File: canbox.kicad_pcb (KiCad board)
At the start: 2 copper layers, 80 x 50 mm, 108 parts, among them J1 Conn_ARM_SWD_NXP, J2 Screw_Terminal_01x02, J3 Screw_Terminal_01x02, J4 Conn_ARM_JTAG_SWD_20, J5 DB9_Male, J7 USB_B_Micro, K2 FTR-K3AB005W, U1 LPC54616J512, U11 MP1582, U3 TJA1102SHN, U5 TJA1051T, U6 TLV70233_SOT23-5, U7 KeyMatrix, U8 ULN2003ADRG3, Y1 12MHz, Y2 32.768k, Y3 25Mhz

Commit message: Fix few bugs, review design
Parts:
- added R11: NC, Resistor_SMD:R_0805_2012Metric_Pad1.15x1.40mm_HandSolder, F.Cu at (49.5, 117.3)
- D1: footprint Package_TO_SOT_SMD:SOT-143 -> Package_TO_SOT_SMD:SOT-143_Handsoldering
- moved L5 1.22 mm to (49.2, 112.5)
- moved C24 0.76 mm to (102.4, 130.0), turned to 180 degrees
- moved L3 0.73 mm to (105.9, 125.6), turned to 90 degrees
- moved R12 0.45 mm to (52.3, 110.9), turned to 90 degrees
- turned D5 to 180 degrees
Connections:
- D5 pad 1: GND -> Net-(C45-Pad1)
- D5 pad 2: Net-(C45-Pad1) -> GND
- J5 pad 1: /CAN/CAN_L -> (no net)
- J5 pad 2: (no net) -> /CAN/CAN_L
- J5 pad 7: (no net) -> /CAN/CAN_H
- J5 pad 8: /CAN/CAN_H -> (no net)
- L5 pad 3: /CAN/CAN_L -> Net-(L5-Pad3)
- L5 pad 4: Net-(L5-Pad4) -> /CAN/CAN_L
- R13 pad 1: Net-(L5-Pad4) -> Net-(L5-Pad3)
- U3 pad 17: /Ethernet/TRX_0_T_N -> /Ethernet/TRX_0_T_P
- U3 pad 18: /Ethernet/TRX_0_T_P -> /Ethernet/TRX_0_T_N
- U3 pad 48: (no net) -> +3V3
- U5 pad 5: (no net) -> Net-(R11-Pad2)
- U5 pad 6: Net-(L5-Pad4) -> Net-(L5-Pad3)
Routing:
- net GND: track 949.1 -> 879.2 mm, vias 59 -> 53
- net 5V: track 192.2 -> 221.6 mm
- net Net-(L5-Pad3): track 0.00 -> 16.7 mm, vias 0 -> 1
- net Net-(L5-Pad4): track 15.6 -> 0.00 mm, vias 1 -> 0
- net /Ethernet/TRX_0_T_N: track 5.14 -> 11.4 mm
- net /CAN/CAN_H: track 24.4 -> 29.6 mm
- net /MCU/3V3_LC: track 77.8 -> 82.6 mm, vias 4 -> 5
- net /Ethernet/TRX_0_P: track 2.98 -> 7.43 mm
- net Net-(R11-Pad2): track 0.00 -> 4.22 mm
- net /Ethernet/TRX_0_T_P: track 6.50 -> 9.89 mm
- net /PowerSupply/D+: track 41.3 -> 38.1 mm
- net /CAN/CAN_L: track 40.3 -> 37.2 mm
- net Net-(C22-Pad1): track 30.2 -> 33.2 mm
- net /Ethernet/TRX_0_N: track 14.1 -> 11.2 mm
- net Net-(L5-Pad2): track 14.1 -> 11.2 mm
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
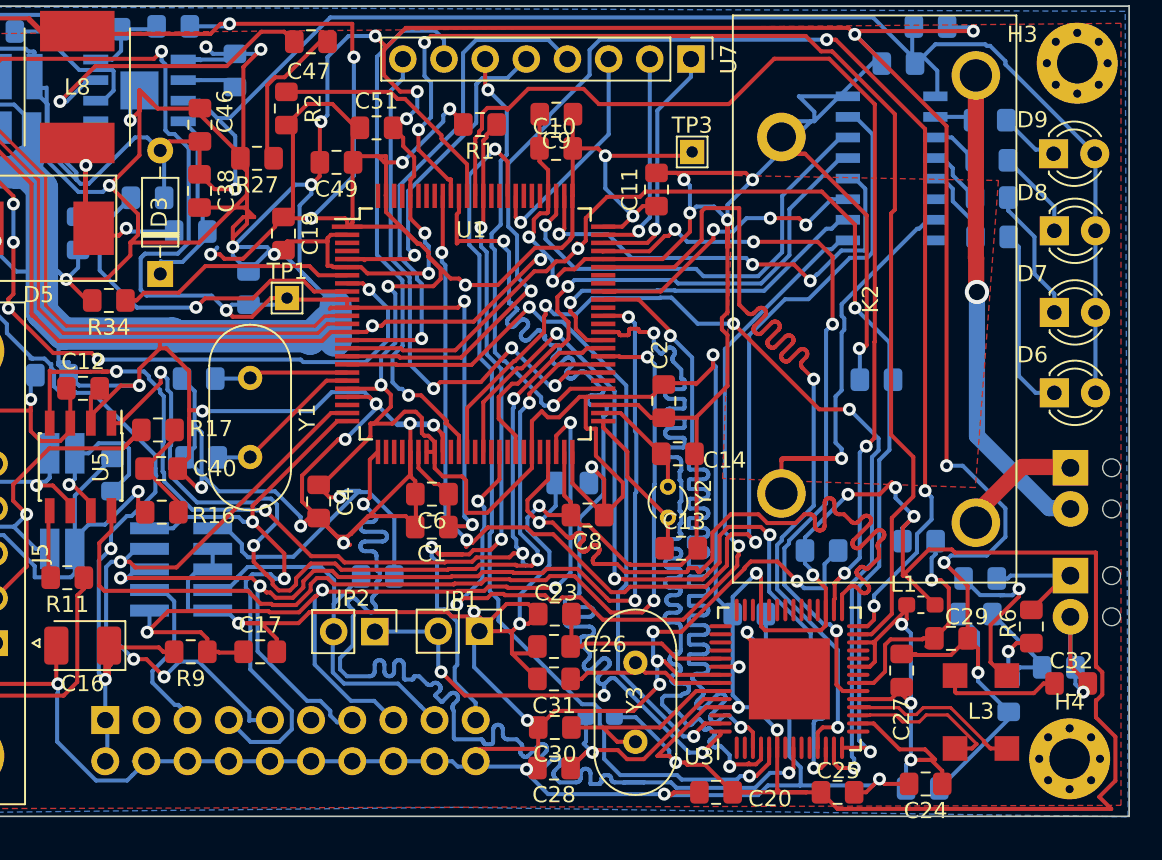
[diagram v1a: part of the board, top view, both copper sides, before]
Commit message: Add solder jumper for termination.
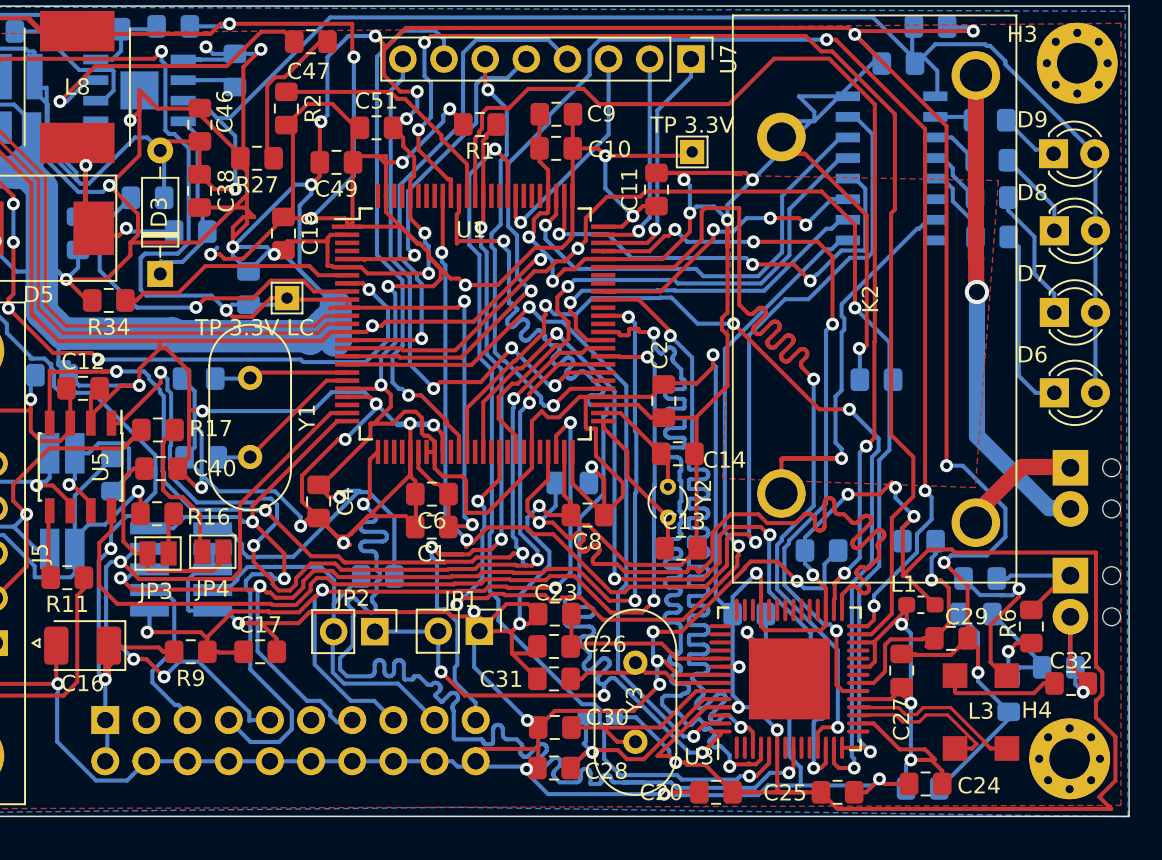
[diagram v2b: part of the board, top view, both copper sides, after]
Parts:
- added JP3: Jumper_NC_Small-Device, Jumper:SolderJumper-2_P1.3mm_Open_Pad1.0x1.5mm, F.Cu at (55.1, 115.8)
- added JP4: Jumper_NC_Small-Device, Jumper:SolderJumper-2_P1.3mm_Open_Pad1.0x1.5mm, F.Cu at (58.5, 115.7)
- TP 3.3V: renamed from TP3
- TP 3.3V LC: renamed from TP1
- moved R16 0.31 mm to (55.0, 113.3)
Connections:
- R16 pad 2: Net-(C40-Pad1) -> Net-(JP3-Pad2)
- R17 pad 2: Net-(C40-Pad1) -> Net-(JP4-Pad1)
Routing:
- net Net-(JP4-Pad1): track 0.00 -> 9.73 mm
- net Net-(C40-Pad1): track 6.72 -> 13.7 mm
- net Net-(C17-Pad1): track 59.3 -> 55.9 mm
- net Net-(J1-Pad4): track 39.5 -> 42.6 mm
- net Net-(JP3-Pad2): track 0.00 -> 2.58 mm

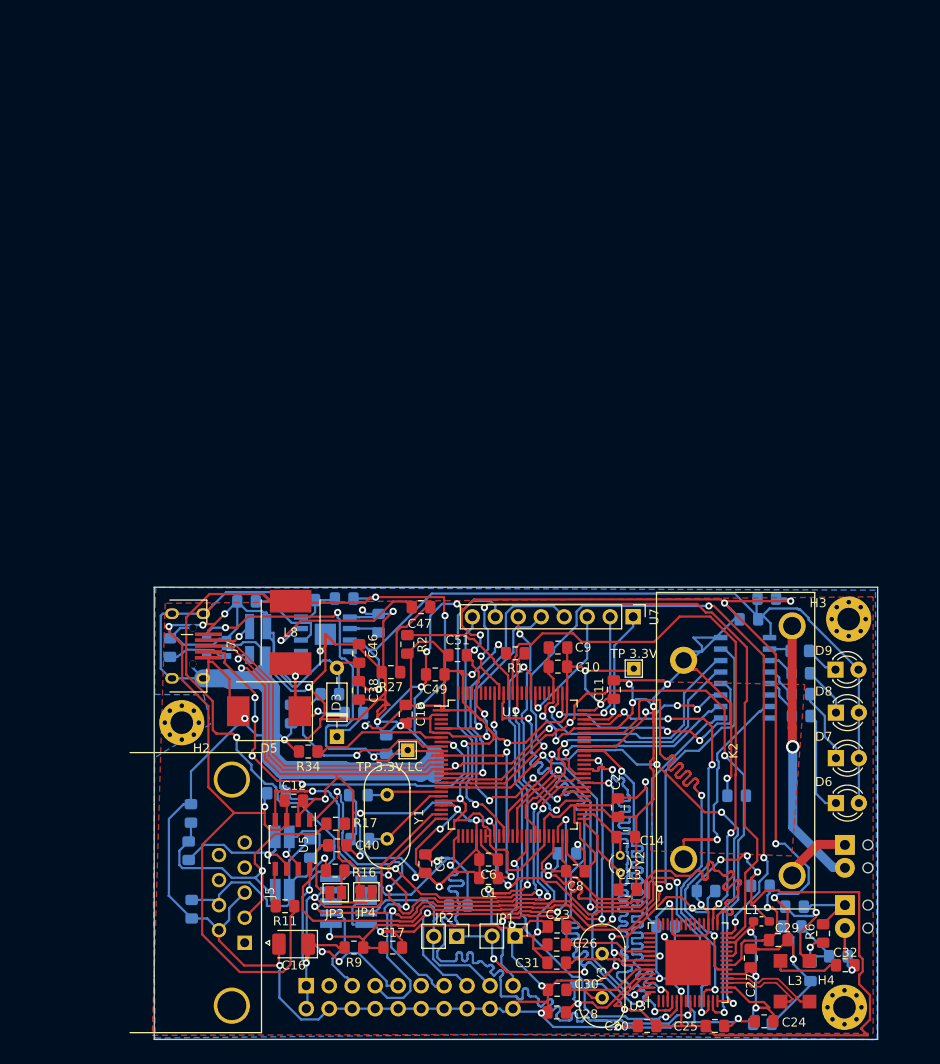
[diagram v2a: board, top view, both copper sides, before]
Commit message: V3 bigger board, RMII instrumentation, inverter
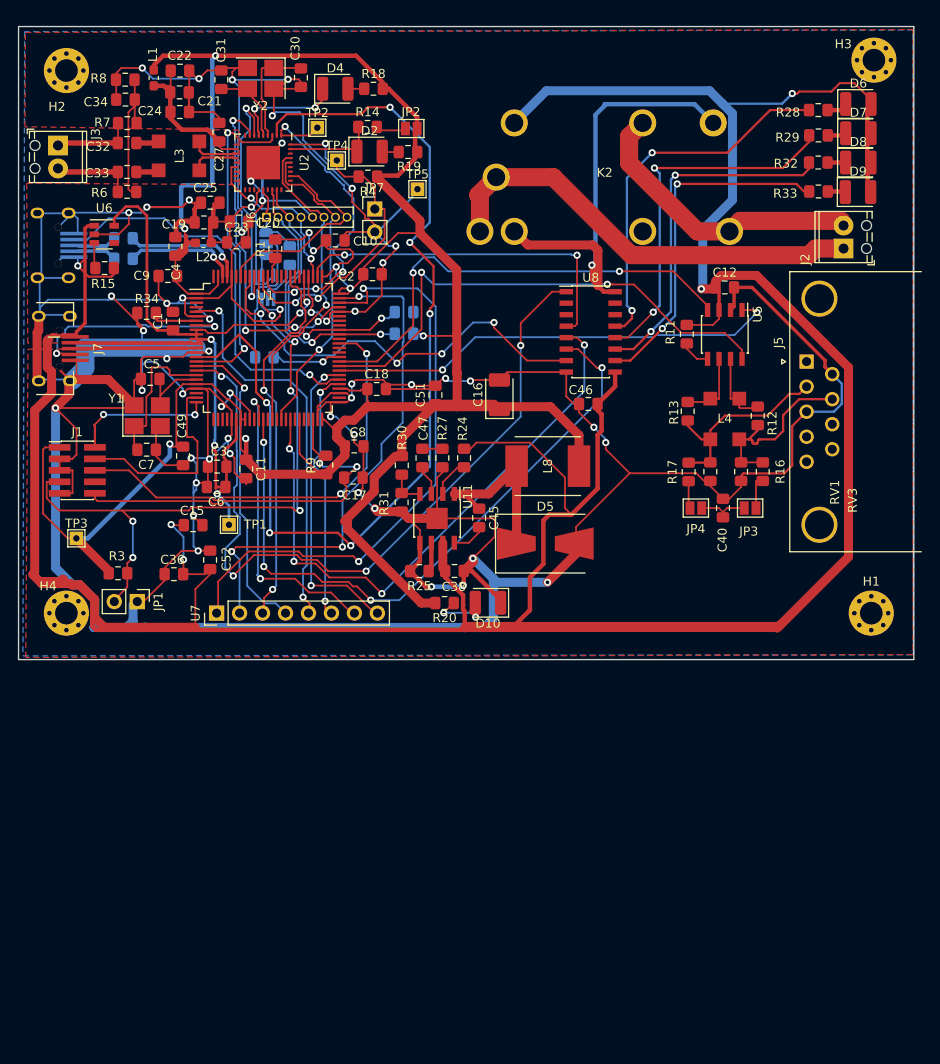
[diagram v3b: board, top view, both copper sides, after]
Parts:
- removed C13, C14: 22p, Capacitor_SMD:C_0805_2012Metric_Pad1.15x1.40mm_HandSolder
- removed C26: 10n, Capacitor_SMD:C_0805_2012Metric_Pad1.15x1.40mm_HandSolder
- removed C28, C29: 100n, Capacitor_SMD:C_0805_2012Metric_Pad1.15x1.40mm_HandSolder
- removed D1: PRTR5V0U2X, Package_TO_SOT_SMD:SOT-143_Handsoldering
- removed D3: 1N4148, Diode_THT:D_DO-35_SOD27_P7.62mm_Horizontal
- removed L5: DLW43MH201XK2L, cypress:DLW43MH201XK2L
- removed R26: 124k, Resistor_SMD:R_0805_2012Metric_Pad1.15x1.40mm_HandSolder
- removed TP 3.3V: TestPoint, TestPoint:TestPoint_THTPad_1.5x1.5mm_Drill0.7mm
- removed TP 3.3V LC: TestPoint, TestPoint:TestPoint_THTPad_1.5x1.5mm_Drill0.7mm
- removed Y3: 25Mhz, Crystal:Crystal_HC49-4H_Vertical
- added D10: LED, LED_SMD:LED_1210_3225Metric, F.Cu at (71.9, 83.7)
- added D2: LED, LED_SMD:LED_1210_3225Metric, F.Cu at (58.8, 33.8)
- added D4: LED, LED_SMD:LED_1210_3225Metric, F.Cu at (55.0, 26.9)
- added H1: H, MountingHole:MountingHole_2.5mm_Pad_Via, F.Cu at (114.3, 84.9)
- added J6: Conn_01x08_Female, Connector_PinHeader_1.27mm:PinHeader_1x08_P1.27mm_Vertical_RMII, F.Cu at (47.4, 41.1)
- added JP5: Jumper_3_Bridged12, Jumper:SolderJumper-3_P1.3mm_Open_RoundedPad1.0x1.5mm, B.Cu at (47.4, 44.0)
- added JP7: MDIO, Connector_PinHeader_2.54mm:PinHeader_1x02_P2.54mm_Vertical, F.Cu at (59.4, 40.2)
- added L4: AE2002, Inductor_SMD:L_CMC_1812, F.Cu at (98.1, 63.4)
- added R14: 2.49k, Resistor_SMD:R_0805_2012Metric_Pad1.15x1.40mm_HandSolder, F.Cu at (58.6, 31.1)
- added R18: 100, Resistor_SMD:R_0805_2012Metric_Pad1.15x1.40mm_HandSolder, F.Cu at (59.3, 26.9)
- added R19: 100, Resistor_SMD:R_0805_2012Metric_Pad1.15x1.40mm_HandSolder, F.Cu at (63.1, 33.9)
- added R20: 100, Resistor_SMD:R_0805_2012Metric_Pad1.15x1.40mm_HandSolder, F.Cu at (67.1, 83.7)
- added R21: 33, Resistor_SMD:R_0805_2012Metric_Pad1.15x1.40mm_HandSolder, B.Cu at (31.6, 43.4)
- added R22: 33, Resistor_SMD:R_0805_2012Metric_Pad1.15x1.40mm_HandSolder, B.Cu at (47.2, 56.6)
- added TP1: TestPoint, TestPoint:TestPoint_THTPad_1.5x1.5mm_Drill0.7mm, F.Cu at (43.3, 75.1)
- added TP2: MDC, TestPoint:TestPoint_THTPad_1.5x1.5mm_Drill0.7mm, F.Cu at (53.0, 31.2)
- added TP3: TestPoint, TestPoint:TestPoint_THTPad_1.5x1.5mm_Drill0.7mm, F.Cu at (26.4, 76.6)
- added TP4: MDIO, TestPoint:TestPoint_THTPad_1.5x1.5mm_Drill0.7mm, F.Cu at (55.2, 34.8)
- added TP5: GND, TestPoint:TestPoint_THTPad_1.5x1.5mm_Drill0.7mm, F.Cu at (64.1, 38.0)
- added U2: DP83TC811R-Q1, cypress:QFN-36_EP_6x6_Pitch0.5mm, F.Cu at (47.1, 35.0)
- C15, C18, C22, C3, C33, C34, C36, C45, C5, C52, C7, L2, R12, R13, R28, R29, R30, R32, R33, R7, RV1, RV3, U6, U8: moved to F.Cu
- C19: value 100n -> 22u
- C20, C27: value 100n -> 10n
- C21: value 100n -> 470n; moved to F.Cu
- C23: value 470n -> 470
- D5: footprint Diode_SMD:D_SMC -> Diode_SMD:D_SMB-SMC_Universal_Handsoldering
- D6, D7, D8, D9: footprint LED_THT:LED_D3.0mm -> LED_SMD:LED_1210_3225Metric
- H2, H3, H4: value MountingHole -> H
- J1: value Conn_ARM_SWD_NXP -> SWD; moved to F.Cu
- J2: value Screw_Terminal_01x02 -> RELAY; moved to F.Cu
- J3: value Screw_Terminal_01x02 -> 100BaseT1; moved to F.Cu
- J4: value Conn_ARM_JTAG_SWD_20 -> USB_B_Micro; footprint Connector_IDC:IDC-Header_2x10_P2.54mm_Vertical -> cypress:MicroUsb
- JP1: value Jumper_NC_Small -> MCD
- JP2: value Jumper_NC_Small -> SLAVE; footprint Connector_PinHeader_2.54mm:PinHeader_1x02_P2.54mm_Vertical -> Jumper:SolderJumper-2_P1.3mm_Open_Pad1.0x1.5mm
- JP3, JP4: value Jumper_NC_Small-Device -> TERM
- R1, R9: value 100k -> 124k
- R10: value 10k -> 2.49k
- R15, R24, R3, R8: value 100k -> 124k; moved to F.Cu
- R2: value 100k -> 33; moved to B.Cu
- R23: value 124k -> 33
- R25: value 200k -> 124k; moved to F.Cu
- R31: value 40.2k -> 39.2k; moved to F.Cu
- R4: value 10k -> 2.49k; moved to F.Cu
- R5: value 1k -> 2.49k
- U11: value MP1582 -> MP1582EN-LF-Z; moved to F.Cu
- U3: value TJA1102SHN -> 74LVC1G04; footprint canbox_nxp_LPC546xx:QFN-56_EP_8.5x8.5_Pitch0.5mm -> Package_TO_SOT_SMD:SOT-353_SC-70-5_Handsoldering; moved to B.Cu
- U5: value TJA1051T -> TJA1051T/3/1J
- Y1: value 12MHz -> 12MHZ; footprint Crystal:Crystal_HC49-4H_Vertical -> Crystal:Crystal_SMD_3225-4Pin_3.2x2.5mm_HandSoldering
- Y2: value 32.768k -> 25 MHz; footprint Crystal:Crystal_DS26_D2.0mm_L6.0mm_Vertical -> Crystal:Crystal_SMD_3225-4Pin_3.2x2.5mm_HandSoldering
- moved R8 124.4 mm to (31.8, 25.9), turned to 180 degrees
- moved C22 123.5 mm to (37.9, 24.9)
- moved R7 121.1 mm to (32.0, 30.7), turned to 0 degrees
- moved J3 120.9 mm to (24.4, 33.2)
- moved C32 120.7 mm to (32.0, 32.9), turned to 0 degrees
- moved C24 119.5 mm to (37.8, 29.5), turned to 0 degrees
- moved C34 117.4 mm to (31.8, 28.1)
- moved L1 115.0 mm to (35.0, 25.7), turned to 270 degrees
- moved L3 113.9 mm to (37.7, 34.3), turned to 0 degrees
- moved R6 112.5 mm to (32.0, 38.3), turned to 0 degrees
- moved C33 109.8 mm to (32.0, 36.1), turned to 180 degrees
- moved C27 108.6 mm to (42.2, 31.7)
- moved C25 106.8 mm to (41.2, 39.5), turned to 180 degrees
- moved C21 106.8 mm to (37.8, 27.3)
- moved C30 104.8 mm to (51.2, 25.7), turned to 270 degrees
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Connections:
- C1 pad 1: /MCU/3V3_LC -> /3V3_LC
- C12 pad 1: 5V -> +5V
- C15 pad 1: 5V -> +5V
- C19 pad 1: +3V3 -> /Ethernet/ETH_3V3
- C20 pad 1: +3V3 -> /Ethernet/ETH_3V3
- C21 pad 1: +3V3 -> Net-(C21-Pad1)
- C22 pad 1: Net-(C22-Pad1) -> Net-(C21-Pad1)
- C23 pad 1: Net-(C23-Pad1) -> /Ethernet/ETH_3V3
- C24 pad 1: Net-(C22-Pad1) -> Net-(C21-Pad1)
- C25 pad 1: +3V3 -> /Ethernet/ETH_3V3
- C27 pad 1: Net-(C22-Pad1) -> Net-(C21-Pad1)
- C3 pad 1: /MCU/3V3_LC -> /3V3_LC
- C36 pad 1: 5V -> +5V
- C38 pad 1: 5V -> +5V
- C46 pad 1: 5V -> +5V
- C52 pad 1: 5V -> +5V
- C6 pad 1: /MCU/3V3_LC -> /3V3_LC
- D6 pad 2: 5V -> +5V
- D7 pad 2: 5V -> +5V
- D8 pad 2: 5V -> +5V
- D9 pad 2: 5V -> +5V
- J1 pad 8: Net-(J1-Pad8) -> (no net)
- J3 pad 1: /Ethernet/TRX_CON0_N -> /Ethernet/TRX_CON0_P
- J3 pad 2: /Ethernet/TRX_CON0_P -> /Ethernet/TRX_CON0_N
- J4 pad 1: +3V3 -> +5V
- J4 pad 2: +3V3 -> /PowerSupply/Slow_D-
- J4 pad 3: (no net) -> /PowerSupply/Slow_D+
- J4 pad 4: GND -> Net-(J4-Pad4)
- J4 pad 5: Net-(J1-Pad8) -> GND
- J7 pad 1: 5V -> +5V
- JP1 pad 2: RX_DV -> Net-(J1-Pad7)
- JP2 pad 1: RX_DV -> +3V3
- JP2 pad 2: Net-(J1-Pad7) -> Net-(JP2-Pad2)
- K2 pad 1: GND -> Net-(K2-Pad1)
- K2 pad 2: Net-(K2-Pad2) -> +5V
- L1 pad 2: Net-(C22-Pad1) -> Net-(C21-Pad1)
- L2 pad 2: Net-(C28-Pad1) -> /Ethernet/ETH_3V3
- L3 pad 1: /Ethernet/TRX_0_T_P -> /Ethernet/TRX_0_P
- L3 pad 2: /Ethernet/TRX_0_T_N -> /Ethernet/TRX_0_N
- L3 pad 3: /Ethernet/TRX_0_N -> /Ethernet/TRX_0_T_N
- L3 pad 4: /Ethernet/TRX_0_P -> /Ethernet/TRX_0_T_P
- R1 pad 1: Net-(J4-Pad19) -> Net-(R1-Pad1)
- R10 pad 1: Net-(R10-Pad1) -> +3V3
- R10 pad 2: GND -> /Ethernet/RGMII_D1
- R11 pad 1: 5V -> +5V
- R15 pad 1: 5V -> +5V
- R2 pad 1: Net-(R2-Pad1) -> /PowerSupply/Slow_D-
- R2 pad 2: +3V3 -> /PowerSupply/USB0_D-
- R23 pad 1: 5V -> /Ethernet/RGMII_CLK
- R24 pad 1: 5V -> +5V
- R4 pad 2: Net-(R4-Pad2) -> /Ethernet/MDIO
- R5 pad 1: Net-(C29-Pad1) -> +3V3
- R5 pad 2: +3V3 -> /Ethernet/RGMII_DO
- U1 pad 10: /MCU/3V3_LC -> /3V3_LC
- U1 pad 11: /MCU/3V3_LC -> /3V3_LC
- U1 pad 16: Net-(R10-Pad1) -> Net-(U1-Pad16)
- U1 pad 26: Net-(U1-Pad26) -> (no net)
- U1 pad 31: /MCU/3V3_LC -> /3V3_LC
- U1 pad 39: /Ethernet/TXD0_L -> /Ethernet/RGMII_TX_D0
- U1 pad 41: Net-(U1-Pad41) -> /Ethernet/RGMII_TX_D1
- U1 pad 47: Net-(R4-Pad2) -> (no net)
- U1 pad 51: Net-(C13-Pad1) -> GND
- U1 pad 52: Net-(C14-Pad1) -> (no net)
- U1 pad 56: (no net) -> Net-(J4-Pad4)
- U1 pad 61: Net-(U1-Pad61) -> Net-(R22-Pad2)
- U1 pad 62: /Ethernet/RXD0_L -> (no net)
- U1 pad 66: /Ethernet/RXD1_L -> /Ethernet/RGMII_D1
- U1 pad 67: Net-(U1-Pad67) -> /Ethernet/RGMII_DO
- U1 pad 70: /Ethernet/TXD1_L -> (no net)
- U1 pad 78: Net-(U1-Pad78) -> /Ethernet/RGMII_DV
- U1 pad 80: (no net) -> /3V3_LC
- U1 pad 84: /Ethernet/RX_CLK_L -> (no net)
- U1 pad 87: Net-(J4-Pad19) -> Net-(R1-Pad1)
- U1 pad 88: Net-(U1-Pad88) -> /Ethernet/MDC
- U1 pad 89: Net-(R2-Pad1) -> /Ethernet/MDIO
- U1 pad 9: Net-(R23-Pad2) -> /3V3_LC
- U1 pad 90: RX_DV -> Net-(J1-Pad7)
- U1 pad 94: (no net) -> /Ethernet/RGMII_TX_EN
- U1 pad 97: (no net) -> /PowerSupply/USB0_D+
- U1 pad 98: (no net) -> /PowerSupply/USB0_D-
- U11 pad 7: 5V -> +5V
- U3 pad 2: (no net) -> Net-(R23-Pad2)
- U3 pad 3: /Ethernet/RXD1_L -> GND
- U3 pad 4: /Ethernet/RXD0_L -> Net-(JP5-Pad3)
- U3 pad 5: /Ethernet/RX_CLK_L -> /Ethernet/ETH_3V3
- U5 pad 3: 5V -> +5V
- U6 pad 1: 5V -> +5V
- U6 pad 5: /MCU/3V3_LC -> /3V3_LC
- U7 pad 4: Net-(U1-Pad15) -> Net-(U1-Pad17)
- U8 pad 1: Net-(U1-Pad41) -> Net-(U1-Pad18)
- U8 pad 15: Net-(K2-Pad2) -> (no net)
- U8 pad 16: (no net) -> Net-(K2-Pad1)
- U8 pad 2: Net-(U1-Pad61) -> (no net)
- U8 pad 3: Net-(U1-Pad67) -> (no net)
- U8 pad 6: Net-(U1-Pad78) -> Net-(U1-Pad37)
- U8 pad 9: 5V -> +5V
- Y1 pad 2: Net-(C5-Pad1) -> GND
- Y2 pad 1: Net-(C14-Pad1) -> Net-(C30-Pad1)
- Y2 pad 2: Net-(C13-Pad1) -> GND
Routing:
- net +5V: track 0.00 -> 414.5 mm, vias 0 -> 5
- net 5V: track 221.6 -> 0.00 mm, vias 5 -> 0
- net GND: track 879.2 -> 716.7 mm
- net +3V3: track 439.4 -> 317.4 mm, vias 26 -> 9
- net RX_DV: track 82.8 -> 0.00 mm, vias 4 -> 0
- net /MCU/3V3_LC: track 82.6 -> 0.00 mm, vias 5 -> 0
- net Net-(U1-Pad15): track 31.7 -> 109.4 mm, vias 1 -> 6
- net Net-(R10-Pad1): track 74.9 -> 0.00 mm, vias 3 -> 0
- net /3V3_LC: track 0.00 -> 71.5 mm, vias 0 -> 5
- net Net-(U1-Pad26): track 70.6 -> 0.00 mm, vias 2 -> 0
- net Net-(U1-Pad88): track 66.1 -> 0.00 mm, vias 2 -> 0
- net /Ethernet/RXD1_L: track 59.8 -> 0.00 mm, vias 2 -> 0
- net /Ethernet/TXD1_L: track 58.1 -> 0.00 mm, vias 2 -> 0
- net /Ethernet/RXD0_L: track 58.0 -> 0.00 mm, vias 2 -> 0
- net /Ethernet/RX_CLK_L: track 57.6 -> 0.00 mm, vias 2 -> 0
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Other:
- board size 80 x 50 mm -> 99 x 70 mm
- net class Default: clearance 0.2 -> 0.127; trace_width 0.25 -> 0.24
- rule trace_clearance: 0.2 -> 0.127
- rule trace_min: 0.2 -> 0.1905
- rule via_min_size: 0.4 -> 0.6

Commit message: Improve PCB, local loopback works - via RMII not
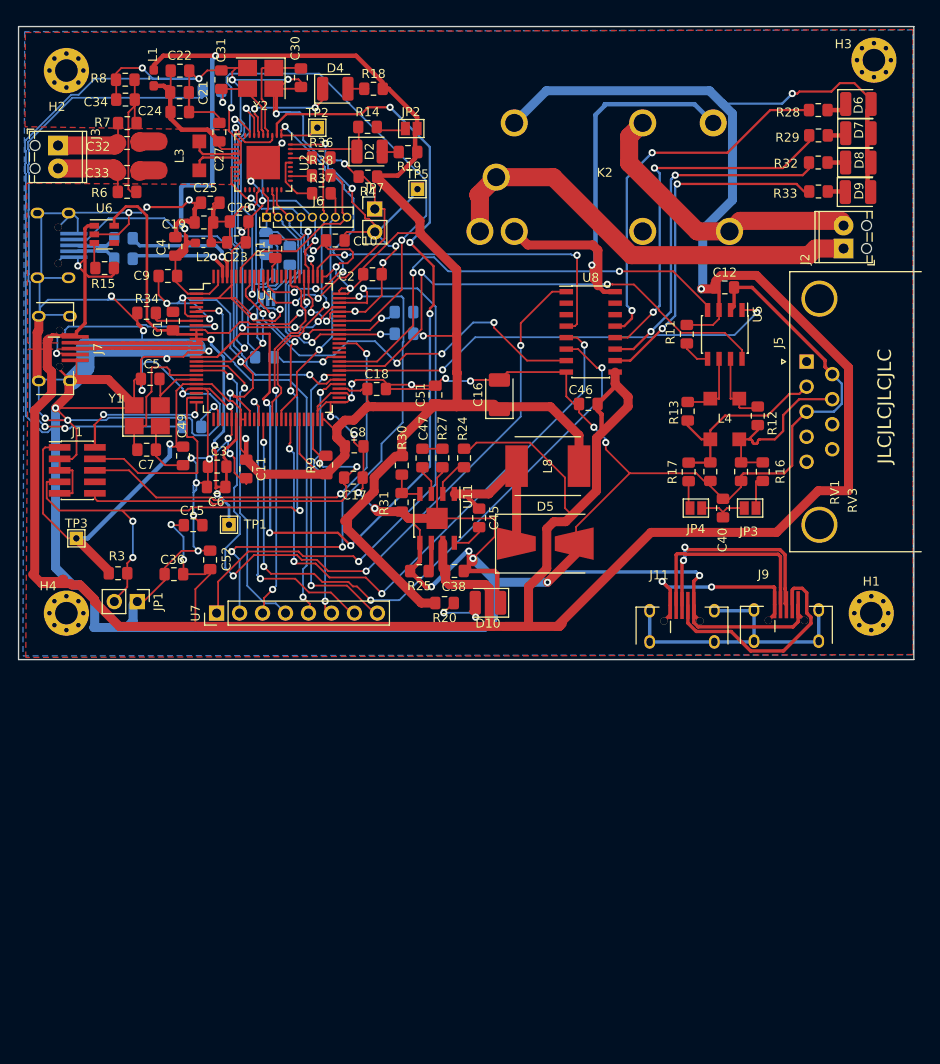
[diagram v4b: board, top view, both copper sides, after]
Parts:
- removed TP4: MDIO, TestPoint:TestPoint_THTPad_1.5x1.5mm_Drill0.7mm
- added J11: USB_B_Micro, cypress:MicroUsb, F.Cu at (93.4, 87.0)
- added J9: USB_B_Micro, cypress:MicroUsb, F.Cu at (104.9, 86.9)
- added R26: NM, Resistor_SMD:R_0805_2012Metric_Pad1.15x1.40mm_HandSolder, B.Cu at (41.4, 27.1)
- added R35: NM, Resistor_SMD:R_0805_2012Metric_Pad1.15x1.40mm_HandSolder, B.Cu at (39.2, 64.3)
- added R36: NM, Resistor_SMD:R_0805_2012Metric_Pad1.15x1.40mm_HandSolder, F.Cu at (53.5, 34.5)
- added R37: NM, Resistor_SMD:R_0805_2012Metric_Pad1.15x1.40mm_HandSolder, F.Cu at (53.5, 38.4)
- added R38: NM, Resistor_SMD:R_0805_2012Metric_Pad1.15x1.40mm_HandSolder, F.Cu at (53.5, 36.5)
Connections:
- J1 pad 8: (no net) -> Net-(J1-Pad8)
- J5 pad 1: (no net) -> Net-(J5-Pad1)
- J5 pad 4: (no net) -> Net-(J5-Pad4)
- J5 pad 5: (no net) -> Net-(J5-Pad5)
- J5 pad 8: (no net) -> Net-(J5-Pad8)
- J5 pad 9: (no net) -> Net-(J5-Pad9)
- K2 pad 5: (no net) -> Net-(K2-Pad5)
- U1 pad 100: (no net) -> Net-(U1-Pad100)
- U1 pad 27: (no net) -> Net-(R35-Pad2)
- U1 pad 28: (no net) -> Net-(U1-Pad28)
- U1 pad 29: (no net) -> Net-(U1-Pad29)
- U1 pad 3: (no net) -> Net-(U1-Pad3)
- U1 pad 4: (no net) -> Net-(U1-Pad4)
- U1 pad 44: (no net) -> Net-(U1-Pad44)
- U1 pad 47: (no net) -> Net-(U1-Pad47)
- U1 pad 52: (no net) -> Net-(U1-Pad52)
- U1 pad 65: (no net) -> Net-(U1-Pad65)
- U1 pad 69: (no net) -> Net-(U1-Pad69)
- U1 pad 70: (no net) -> Net-(U1-Pad70)
- U1 pad 82: (no net) -> Net-(U1-Pad82)
- U1 pad 85: (no net) -> Net-(U1-Pad85)
- U1 pad 93: (no net) -> Net-(U1-Pad93)
- U1 pad 95: (no net) -> Net-(U1-Pad95)
- U2 pad 14: (no net) -> Net-(U1-Pad69)
- U2 pad 29: /Ethernet/RGMII_TX_EN -> Net-(R38-Pad1)
- U2 pad 32: /Ethernet/RGMII_TX_D1 -> Net-(R37-Pad1)
- U2 pad 33: /Ethernet/RGMII_TX_D0 -> Net-(R36-Pad1)
- U6 pad 4: (no net) -> Net-(U6-Pad4)
- U8 pad 14: (no net) -> Net-(U8-Pad14)
- U8 pad 15: (no net) -> Net-(U8-Pad15)
- U8 pad 2: (no net) -> Net-(U8-Pad2)
- U8 pad 3: (no net) -> Net-(U8-Pad3)
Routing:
- net GND: track 716.7 -> 891.5 mm, vias 53 -> 60
- net Net-(R26-Pad2): track 0.00 -> 69.7 mm, vias 0 -> 2
- net Net-(U1-Pad69): track 0.00 -> 59.5 mm, vias 0 -> 2
- net Net-(J11-Pad6): track 0.00 -> 33.5 mm
- net +5V: track 414.5 -> 383.8 mm
- net Net-(J11-Pad4): track 0.00 -> 25.2 mm
- net Net-(J11-Pad3): track 0.00 -> 23.6 mm, vias 0 -> 2
- net Net-(J11-Pad2): track 0.00 -> 22.6 mm
- net Net-(J11-Pad1): track 0.00 -> 21.7 mm, vias 0 -> 2
- net /Ethernet/TRX_CON0_P: track 8.51 -> 17.9 mm
- net /Ethernet/RGMII_TX_D1: track 35.0 -> 27.9 mm
- net /Ethernet/TRX_CON0_N: track 8.42 -> 15.1 mm
- net Net-(R37-Pad1): track 0.00 -> 6.10 mm
- net Net-(R35-Pad2): track 0.00 -> 4.43 mm, vias 0 -> 1
- net /Ethernet/TRX_0_P: track 2.50 -> 5.51 mm
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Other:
- board text added: "JLCJLCJLCJLC"

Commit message: V4 PCB Release
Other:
- board text added: "CANBOX LPC54616 V4"
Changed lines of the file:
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@@
   (general
     (thickness 1.6)
-    (drawings 5)
+    (drawings 6)
     (tracks 1964)
     (modules 125)
@@
     )
   )
+  (gr_text "CANBOX  LPC54616 V4" (at 89.16504 24.03504) (layer "F.SilkS")
+    (effects (font (size 1.5 1.5) (thickness 0.3)))
+  )
   (gr_text "JLCJLCJLCJLC" (at 115.77504 62.00504 90) (layer "F.SilkS")
